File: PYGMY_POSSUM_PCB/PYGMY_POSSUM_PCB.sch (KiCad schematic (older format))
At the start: 26 parts, among them J1 Conn_PIC_ICSP_ICD, J2 USB_B_Micro, Q1 2N7002, Q2 AO3401A, Q3 2N7002, SW1 SW_SPST, U1 PIC16F18324-xSL, U2 AMS1117-3.3, U3 IP4220CZ6, U4 CH340G, Y1 12MHz

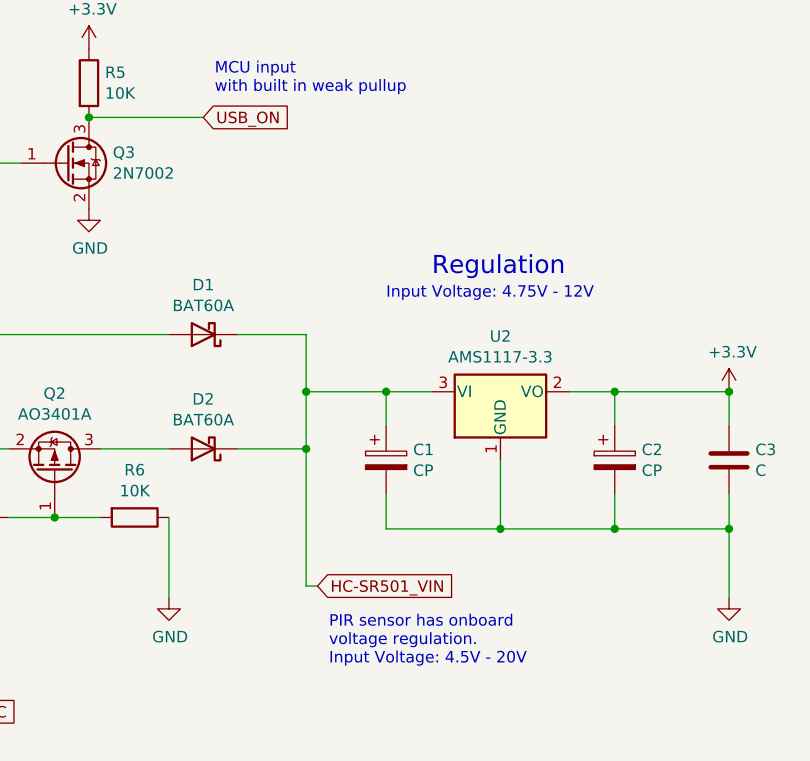
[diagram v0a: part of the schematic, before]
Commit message: added bulk of components
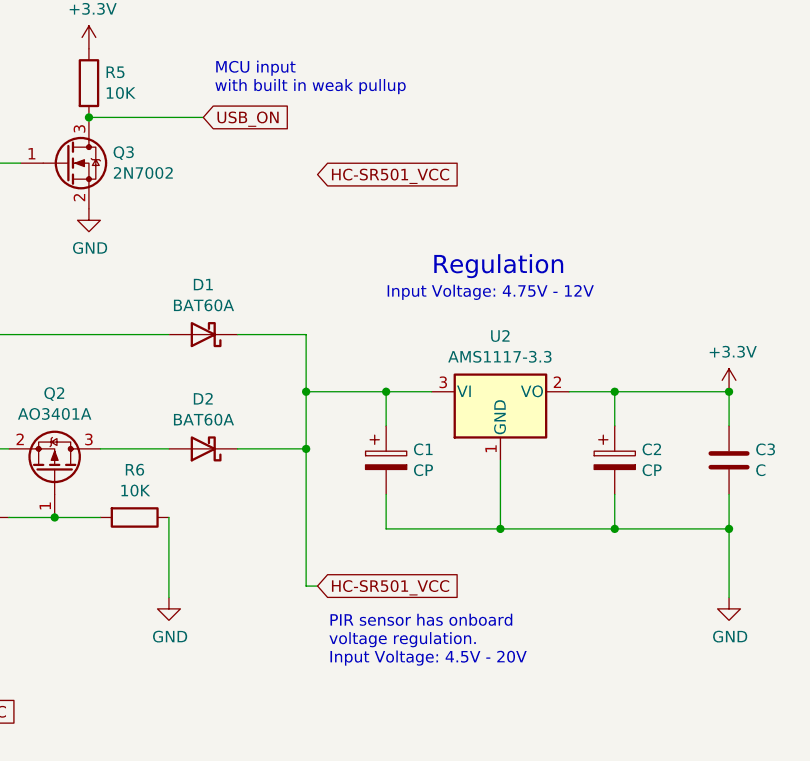
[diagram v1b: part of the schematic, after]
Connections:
- net labels added: HC-SR501_VCC
- net labels removed: HC-SR501_VIN
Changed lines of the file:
@@
 $EndComp
 Text GLabel 4000 3350 2    50   Input ~ 0
-HC-SR501_VIN
+HC-SR501_VCC
 Wire Wire Line
 	4000 3350 3950 3350
@@
 Text GLabel 10600 1400 2    50   Input ~ 0
 PIC_Rx
+Text GLabel 4000 1550 2    50   Input ~ 0
+HC-SR501_VCC
 $EndSCHEMATC

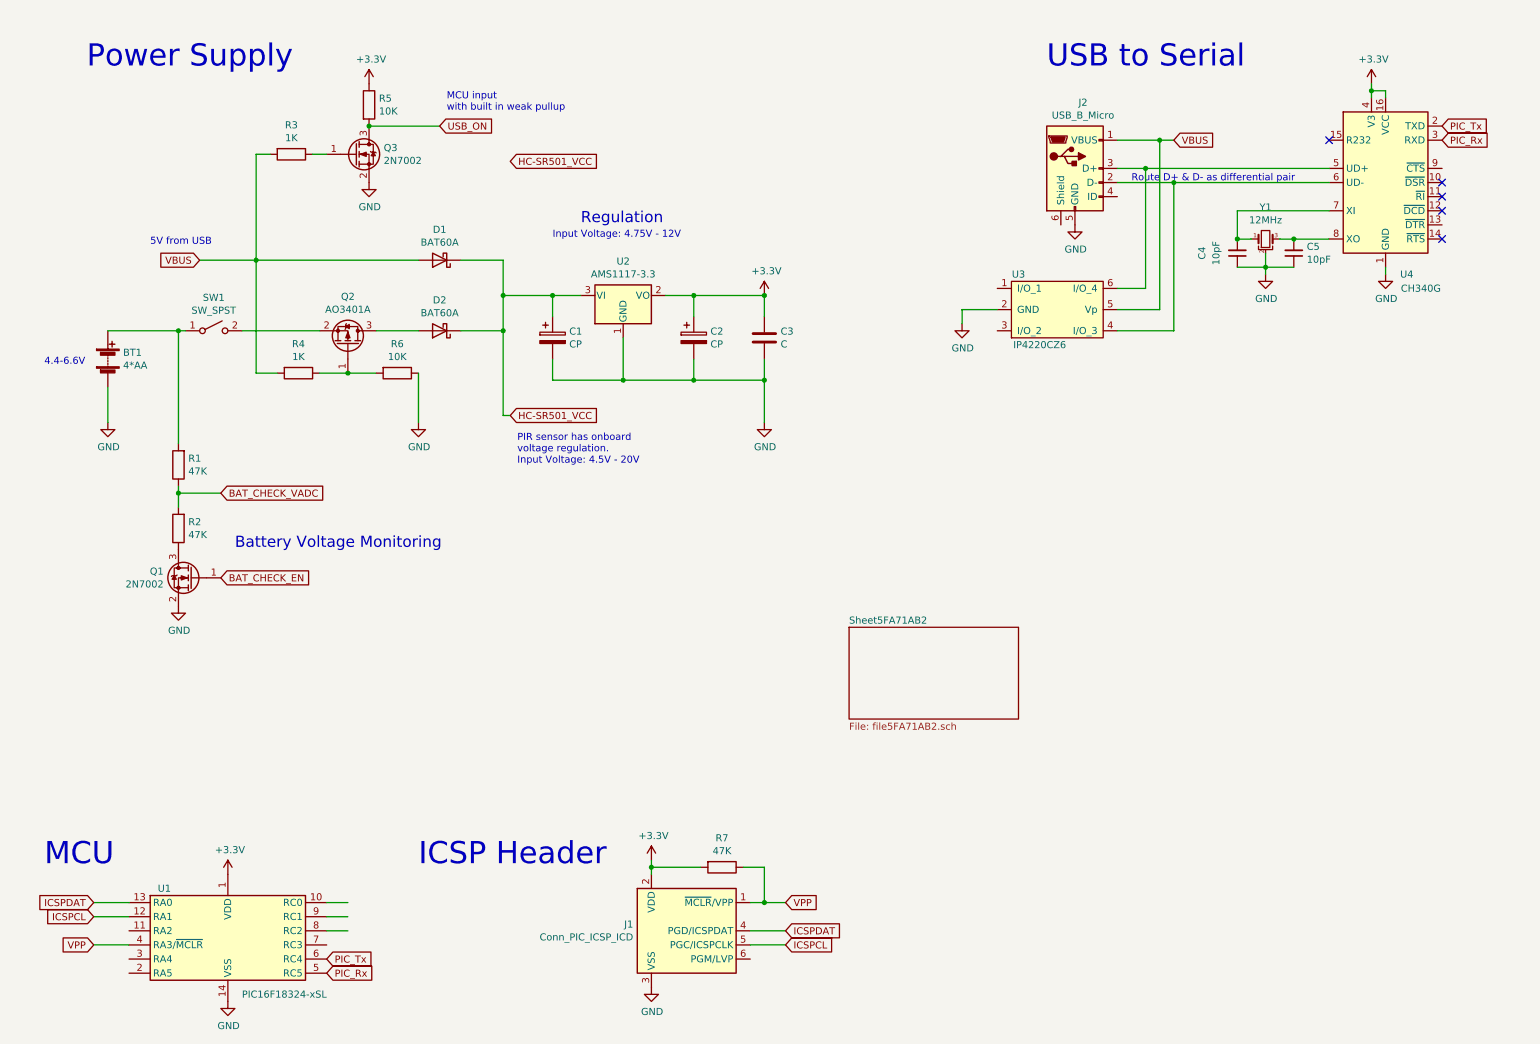
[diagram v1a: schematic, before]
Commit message: Added OR logic to power supply. Added all external devices Upgraded MCU to PIC16F18344 to allow for aditional IO.
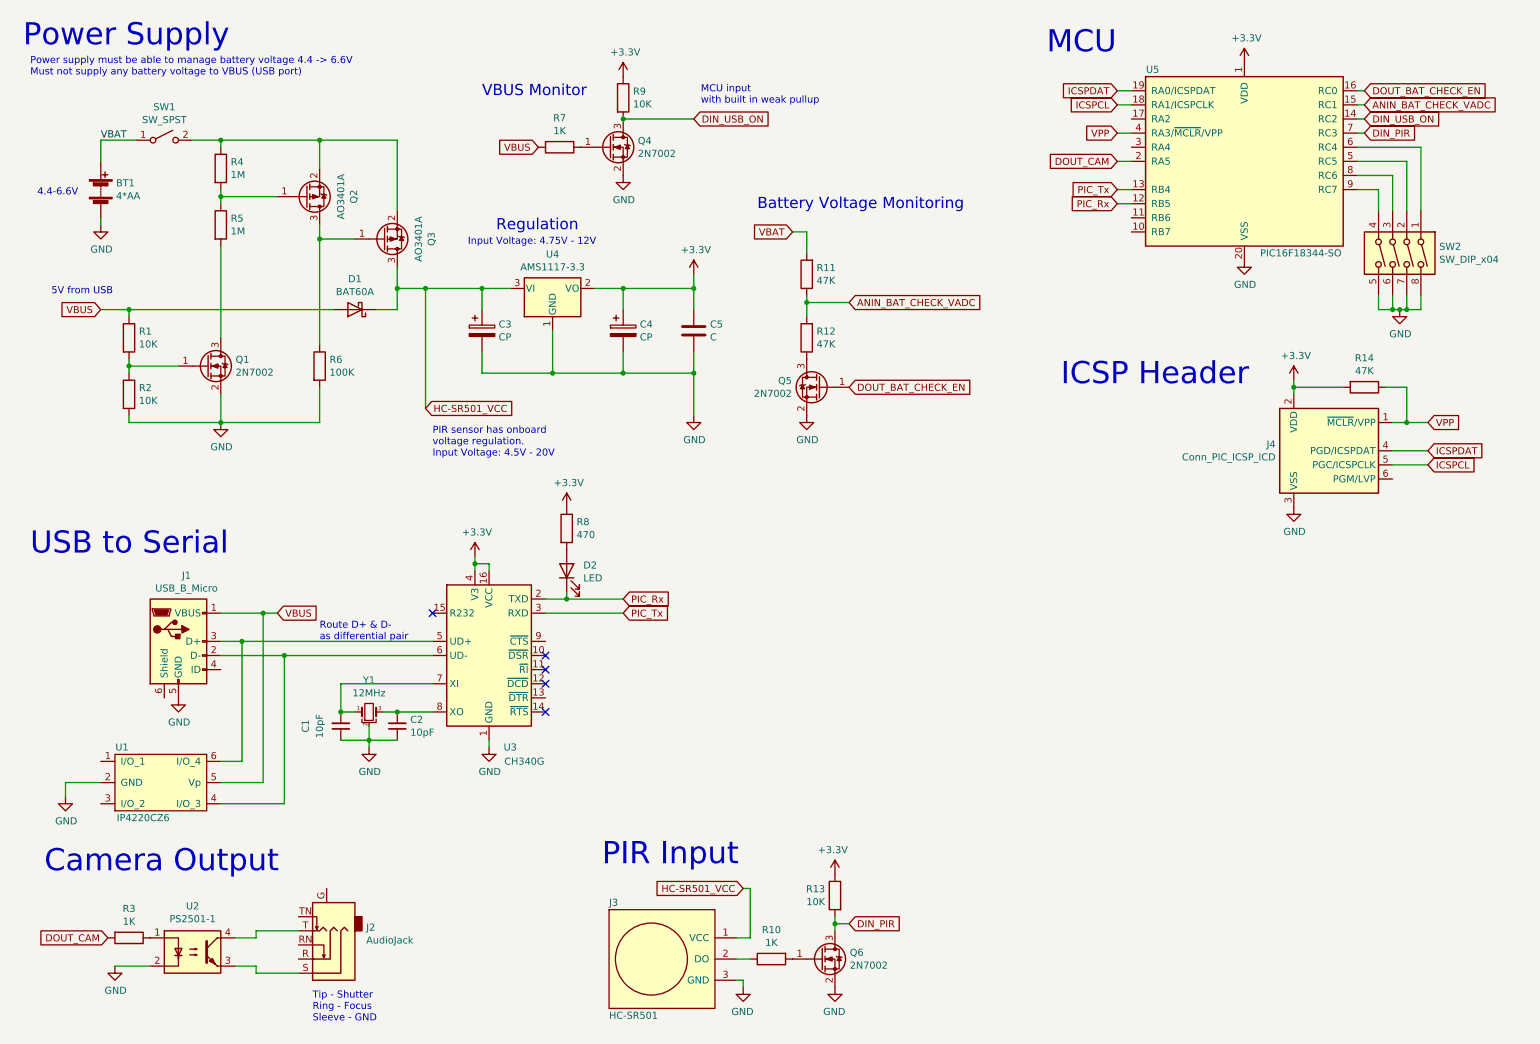
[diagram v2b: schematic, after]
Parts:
- removed C1, C2: CP, symbol Device:CP
- removed C3: C, symbol Device:C
- removed D2: BAT60A, Diode_SMD:D_SOD-323, symbol Diode:BAT60A
- removed Q3: 2N7002, Package_TO_SOT_SMD:SOT-23, symbol Transistor_FET:2N7002
- removed U1: PIC16F18324-xSL, Package_SO:SOIC-14_3.9x8.7mm_P1.27mm, symbol MCU_Microchip_PIC16:PIC16F18324-xSL
- removed U2: AMS1117-3.3, Package_TO_SOT_SMD:SOT-223-3_TabPin2, symbol Regulator_Linear:AMS1117-3.3
- added C3, C4: CP, symbol Device:CP
- added C5: C, symbol Device:C
- added D2: LED, symbol Device:LED
- added J2: AudioJack, Connector_Audio:Jack_3.5mm_Ledino_KB3SPRS_Horizontal, symbol Connector:AudioJack3_Ground_SwitchTR
- added J3: HC-SR501, PIC_CAM_TRAP:HC-SR501, symbol BANKSIA_BYTES_SYMBOLS:HC-SR501
- added Q3: AO3401A, Package_TO_SOT_SMD:SOT-23, symbol Transistor_FET:AO3401A
- added Q4, Q5, Q6: 2N7002, Package_TO_SOT_SMD:SOT-23, symbol Transistor_FET:2N7002
- added R10, R7: 1K, Resistor_SMD:R_0805_2012Metric, symbol Device:R
- added R11, R12: 47K, Resistor_SMD:R_0805_2012Metric, symbol Device:R
- added R13, R9: 10K, Resistor_SMD:R_0805_2012Metric, symbol Device:R
- added R8: 470, Resistor_SMD:R_0805_2012Metric, symbol Device:R
- added SW2: SW_DIP_x04, symbol Switch:SW_DIP_x04
- added U2: PS2501-1, Package_SO:SOIC-4_4.55x2.6mm_P1.27mm, symbol BANKSIA_BYTES_SYMBOLS:PS2501-1
- added U4: AMS1117-3.3, Package_TO_SOT_SMD:SOT-223-3_TabPin2, symbol Regulator_Linear:AMS1117-3.3
- added U5: PIC16F18344-SO, Package_SO:SOIC-20W_7.5x12.8mm_P1.27mm, symbol MCU_Microchip_PIC16:PIC16F18344-SO
- R1, R2: value 47K -> 10K; footprint (none) -> Resistor_SMD:R_0805_2012Metric; LCSC (none) -> C17414
- R14: renamed from R7; footprint (none) -> Resistor_SMD:R_0805_2012Metric
- R3: footprint (none) -> Resistor_SMD:R_0805_2012Metric; LCSC (none) -> C17513
- R4: value 1K -> 1M; footprint (none) -> Resistor_SMD:R_0805_2012Metric
- R5: value 10K -> 1M; footprint (none) -> Resistor_SMD:R_0805_2012Metric
- R6: value 10K -> 100K; footprint (none) -> Resistor_SMD:R_0805_2012Metric
- Y1: footprint (none) -> Crystal:Crystal_SMD_3225-4Pin_3.2x2.5mm; LCSC (none) -> C9002
- renumbered C4 to C1, C5 to C2, J2 to J1, J1 to J4, U3 to U1, U4 to U3
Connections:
- net labels added: ANIN_BAT_CHECK_VADC, DIN_PIR, DIN_USB_ON, DOUT_BAT_CHECK_EN, DOUT_CAM, VBAT
- net labels removed: BAT_CHECK_EN, BAT_CHECK_VADC, USB_ON
- wire segments 84 -> 137
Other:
- note added: "Camera Output"
- note added: "PIR Input"
- note added: "Power supply must be able to manage battery voltage 4.4 -> 6.6V\nMust not supply any battery voltage to VBUS (USB port)"
- note added: "Route D+ & D- \nas differential pair"
- note added: "Tip - Shutter\nRing - Focus\nSleeve - GND"
- note added: "VBUS Monitor"
- note removed: "Route D+ & D- as differential pair"
- moved on the sheet: C1, C2, J1, J4, R14, U1, U3, Y1

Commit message: Updates
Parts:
- removed D2: LED, symbol Device:LED
- removed R8: 470, Resistor_SMD:R_0805_2012Metric, symbol Device:R
- added C1: 0.1uF, Capacitor_SMD:C_0603_1608Metric, symbol Device:C_Small
- added H1, H2, H3, H4: MountingHole_Pad, MountingHole:MountingHole_3mm_Pad_Via, symbol Mechanical:MountingHole_Pad
- added R5: 1K, Resistor_SMD:R_0805_2012Metric, symbol Device:R
- added TP1: TestPoint, TestPoint:TestPoint_Pad_D1.0mm, symbol Connector:TestPoint
- added TP2: T, TestPoint:TestPoint_Pad_2.5x2.5mm, symbol Connector:TestPoint
- added TP3: R, TestPoint:TestPoint_Pad_2.5x2.5mm, symbol Connector:TestPoint
- added TP4: S, TestPoint:TestPoint_Pad_2.5x2.5mm, symbol Connector:TestPoint
- added U3: PS2501-1, Package_SO:SOIC-4_4.55x2.6mm_P1.27mm, symbol BANKSIA_BYTES_SYMBOLS:PS2501-1
- BT1: footprint (none) -> BANKSIA_BYTES_FOOTPRINTS:BatteryHolder_Keystone_2462_2xAA; EL14 (none) -> 1650684; MANUFACTURER (none) -> KEYSTONE; MPN (none) -> 2477; Package (none) -> PTH; Type (none) -> PTH
- C2: renamed from C1; footprint (none) -> Capacitor_SMD:C_0603_1608Metric; LCSC (none) -> C1634; Package (none) -> 0603; Type (none) -> SMD
- C3: renamed from C2; footprint (none) -> Capacitor_SMD:C_0603_1608Metric; LCSC (none) -> C1634; Package (none) -> 0603; Type (none) -> SMD
- C4: renamed from C3; value CP -> CP10u; footprint (none) -> Capacitor_SMD:CP_Elec_4x3.9; LCSC (none) -> C134721; Package (none) -> SMD-ECAP-4x5.3; Type (none) -> SMD
- C5: renamed from C4; value CP -> CP10u; footprint (none) -> Capacitor_SMD:CP_Elec_4x3.9; LCSC (none) -> C134721; Package (none) -> SMD-ECAP-4x5.3; Type (none) -> SMD
- C6: renamed from C5; value C -> 0.1uF; footprint (none) -> Capacitor_SMD:C_0603_1608Metric; LCSC (none) -> C14663; Package (none) -> 0603; Type (none) -> SMD
- D3: renamed from D1; value BAT60A -> BAT60B; LCSC (none) -> C514095; Package (none) -> SOD-323; Type (none) -> SMD
- J1: renamed from J3; footprint PIC_CAM_TRAP:HC-SR501 -> BANKSIA_BYTES_FOOTPRINTS:HC-SR501; LCSC (none) -> -; MANUFACTURER (none) -> -; MPN (none) -> -; Package (none) -> -; Type (none) -> -
- J2: footprint Connector_Audio:Jack_3.5mm_Ledino_KB3SPRS_Horizontal -> Connector_Audio:Jack_3.5mm_CUI_SJ-3523-SMT_Horizontal; symbol Connector:AudioJack3_Ground_SwitchTR -> Connector:AudioJack3; MANUFACTURER (none) -> CUI Devices; MPN (none) -> SJ-3523-SMT-TR; Type (none) -> SMD
- J3: renamed from J1; footprint (none) -> Connector_USB:USB_Micro-B_Molex-105017-0001; MANUFACTURER (none) -> Molex; MPN (none) -> 105017-0001; Type (none) -> PTH / SMD
- J4: footprint (none) -> Connector_PinHeader_2.54mm:PinHeader_1x06_P2.54mm_Vertical; symbol Connector:Conn_PIC_ICSP_ICD -> BANKSIA_BYTES_SYMBOLS:PIC_ICSP; MANUFACTURER (none) -> -; Package (none) -> -; Type (none) -> -
- Q1: renamed from Q6; LCSC (none) -> C8545; MANUFACTURER (none) -> Changjiang Electronics Tech (CJ); MPN (none) -> 2N7002; Package (none) -> SOT-23; Type (none) -> SMD
- Q2: renamed from Q4; LCSC (none) -> C8545; MANUFACTURER (none) -> Changjiang Electronics Tech (CJ); MPN (none) -> 2N7002; Package (none) -> SOT-23; Type (none) -> SMD
- Q3: renamed from Q2; MANUFACTURER (none) -> Alpha & Omega Semicon; MPN (none) -> AO3401A; Package (none) -> SOT-23; Type (none) -> SMD
- Q4: renamed from Q3; MANUFACTURER (none) -> Alpha & Omega Semicon; MPN (none) -> AO3401A; Package (none) -> SOT-23; Type (none) -> SMD
- Q5: LCSC (none) -> C8545; MANUFACTURER (none) -> Changjiang Electronics Tech (CJ); MPN (none) -> 2N7002; Package (none) -> SOT-23; Type (none) -> SMD
- Q6: renamed from Q1; LCSC (none) -> C8545; MANUFACTURER (none) -> Changjiang Electronics Tech (CJ); MPN (none) -> 2N7002; Package (none) -> SOT-23; Type (none) -> SMD
- R1: renamed from R13; MANUFACTURER (none) -> -; Package (none) -> 0805; Type (none) -> SMD
- R10: renamed from R14; LCSC (none) -> C17713; MANUFACTURER (none) -> -; Package (none) -> 0805; Type (none) -> SMD
- R11: LCSC (none) -> C17713; MANUFACTURER (none) -> -; Package (none) -> 0805; Type (none) -> SMD
- R12: renamed from R5; LCSC (none) -> C17514; MANUFACTURER (none) -> -; Package (none) -> 0805; Type (none) -> SMD
- R13: renamed from R12; LCSC (none) -> C17713; MANUFACTURER (none) -> -; Package (none) -> 0805; Type (none) -> SMD
- R14: renamed from R1; MANUFACTURER (none) -> -; Package (none) -> 0805; Type (none) -> SMD
- R15: renamed from R6; LCSC (none) -> C17407; MANUFACTURER (none) -> -; Package (none) -> 0805; Type (none) -> SMD
- R16: renamed from R2; MANUFACTURER (none) -> -; Package (none) -> 0805; Type (none) -> SMD
- R4: renamed from R10; MANUFACTURER (none) -> -; Package (none) -> 0805; Type (none) -> SMD
- R6: renamed from R3; MANUFACTURER (none) -> -; Package (none) -> 0805; Type (none) -> SMD
- R7: renamed from R9; MANUFACTURER (none) -> -; Package (none) -> 0805; Type (none) -> SMD
- R8: renamed from R7; MANUFACTURER (none) -> -; Package (none) -> 0805; Type (none) -> SMD
- R9: renamed from R4; LCSC (none) -> C17514; MANUFACTURER (none) -> -; Package (none) -> 0805; Type (none) -> SMD
- SW1: renamed from SW2; footprint (none) -> Button_Switch_SMD:SW_DIP_SPSTx04_Slide_6.7x11.72mm_W8.61mm_P2.54mm_LowProfile; EL14 (none) -> 9472037; MANUFACTURER (none) -> MULTICOMP PRO; MPN (none) -> MCDM(R)-04-T; Type (none) -> SMD
- SW2: renamed from SW1; footprint (none) -> Button_Switch_THT:SW_CuK_JS202011AQN_DPDT_Angled; EL14 (none) -> 2435145; MANUFACTURER (none) -> C & K COMPONENTS; MPN (none) -> JS202011AQN; Type (none) -> PTH
- U1: renamed from U5; footprint Package_SO:SOIC-20W_7.5x12.8mm_P1.27mm -> Package_SO:SSOP-20_5.3x7.2mm_P0.65mm; symbol MCU_Microchip_PIC16:PIC16F18344-SO -> BANKSIA_BYTES_SYMBOLS:PIC16F18344-SOIC; LCSC (none) -> C144347; MANUFACTURER (none) -> MICROCHIP; MPN (none) -> PIC16F18344-E/SS; Type (none) -> SMD
- U2: renamed from U3; symbol Interface_USB:CH340G -> BANKSIA_BYTES_SYMBOLS:CH340G; MANUFACTURER (none) -> Jiangsu Qin Heng; MPN (none) -> CH340G; Package (none) -> SOIC-16; Type (none) -> SMD
- U4: renamed from U1; footprint (none) -> BANKSIA_BYTES_FOOTPRINTS:SOT457; LCSC (none) -> C282546; MANUFACTURER (none) -> Nexperia; MPN (none) -> IP4220CZ6,125; Package (none) -> SOT457; Type (none) -> SMD
- U5: renamed from U2; MANUFACTURER (none) -> RENESAS; Package (none) -> Package_SO:SOIC-4_4.55x2.6mm_P1.27mm; Type (none) -> SMD
- U6: renamed from U4; LCSC (none) -> C6186; Package (none) -> SOT-223-3; Type (none) -> SMD
- Y1: Package (none) -> SMD-3225_4P; Type (none) -> SMD
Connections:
- net +3V3: now also C1.2
- net DIN_PIR: now also U1.2 (RA5); no longer U1.7 (RC3)
- net DIN_USB_ON: now also U1.15 (RC1); no longer U1.14 (RC2)
- net DOUT_BAT_CHECK_EN: now also U1.17 (RA2); no longer U1.16 (RC0)
- net GND: now also R6.2, C1.1, H1.1, H2.1, H3.1, H4.1, R5.2; no longer U5.2
- net D+: now reaches J3.3 (D+), U2.5 (UD+), U4.6 (I/O_4)
- net D-: now reaches J3.2 (D-), U2.6 (UD-), U4.4 (I/O_3)
- net Xi: now reaches C2.2, U2.7 (XI), Y1.1
- net Xo: now reaches C3.2, U2.8 (XO), Y1.3
- net at J2.R: now also U5.4, TP3.1
- net at J2.S, U5.3: now also TP4.1, U3.3
- net at J2.T: now also TP2.1, U3.4; no longer U5.4
- net at R6.1: now also U5.2; no longer U5.1
- net DO: now reaches J1.2 (DO), R4.1
- net DOUT_CAM_F: now reaches U1.10 (RB7)
- net DOUT_CAM_F: now also U5.1
- net TP_CLK: now reaches U1.3 (RA4)
- net TP_CLK: now also TP1.1
- net DIP1: now reaches U1.5 (RC5)
- net DIP1: now also SW1.4; no longer SW1.2
- net DIP2: now reaches U1.6 (RC4)
- net DIP2: now also SW1.3; no longer SW1.1
- net DIP4: now reaches U1.8 (RC6)
- net DIP4: now also SW1.1; no longer SW1.3
- net DOUT_CAM_S: now reaches U1.9 (RC7)
- net DOUT_CAM_S: now also U3.1; no longer SW1.4
- net ANIN_BAT_CHECK_VADC renamed ANIN_BAT_CHECK
- net ANIN_BAT_CHECK: now also U1.16 (RC0); no longer U1.15 (RC1)
- removed net DOUT_CAM: R6.2, U1.2 (RA5)
- new net: R5.1, U3.2
- new net DIP3: SW1.2, U1.7 (RC3)
- no-connect marks 5 -> 10
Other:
- note added: "Allows user to \ninstall own output"
- note added: "Battery \nVoltage Monitoring"
- note added: "ICSP"
- note added: "Mounting Holes\n"
- note added: "Route as differential pair"
- note added: "User\ninput"
- note removed: "Battery Voltage Monitoring"
- note removed: "ICSP Header"
- note removed: "Route D+ & D- \nas differential pair"
- moved on the sheet: BT1, C2, C3, C4, C5, C6, D3, J1, J3, J4, Q1, Q2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
